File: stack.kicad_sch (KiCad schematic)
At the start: 108 parts, among them CN1 10nF, CN2 10nF, CN3 10nF, CN4 10nF, CN5 10nF, CN6 10nF, CN7 10nF, J5 CELLS, J6 TEMP0, J7 TEMP1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

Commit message: pre production
- footprints change
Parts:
- C11: footprint Capacitor_SMD:C_1206_3216Metric -> Capacitor_SMD:C_1210_3225Metric
- Fa0, Fa1, Fa10, Fa11, Fa12, Fa13, Fa14, Fa2, Fa3, Fa4, Fa5, Fa6, Fa7, Fa8, Fa9: footprint Fuse:Fuse_0805_2012Metric -> Fuse:Fuse_1206_3216Metric
- R3: footprint Resistor_SMD:R_0603_1608Metric -> Resistor_SMD:R_0805_2012Metric
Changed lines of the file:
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@@
       (effects (font (size 1.27 1.27)) hide)
     )
-    (property "Footprint" "Fuse:Fuse_0805_2012Metric" (id 2) (at 60.96 29.972 90)
+    (property "Footprint" "Fuse:Fuse_1206_3216Metric" (id 2) (at 60.96 29.972 90)
       (effects (font (size 1.27 1.27)) hide)
     )
@@
       (effects (font (size 1.27 1.27)) hide)
     )
-    (property "Footprint" "Fuse:Fuse_0805_2012Metric" (id 2) (at 38.1 32.512 90)
+    (property "Footprint" "Fuse:Fuse_1206_3216Metric" (id 2) (at 38.1 32.512 90)
       (effects (font (size 1.27 1.27)) hide)
     )
@@
       (effects (font (size 1.27 1.27)) hide)
     )
-    (property "Footprint" "Fuse:Fuse_0805_2012Metric" (id 2) (at 38.1 29.972 90)
+    (property "Footprint" "Fuse:Fuse_1206_3216Metric" (id 2) (at 38.1 29.972 90)
       (effects (font (size 1.27 1.27)) hide)
     )
@@
     (property "Reference" "R3" (id 0) (at 69.85 128.27 90))
     (property "Value" "100R" (id 1) (at 69.85 129.54 90))
-    (property "Footprint" "Resistor_SMD:R_0603_1608Metric" (id 2) (at 69.85 125.73 0)
+    (property "Footprint" "Resistor_SMD:R_0805_2012Metric" (id 2) (at 69.85 125.73 0)
       (effects (font (size 1.27 1.27)) hide)
     )
@@
       (effects (font (size 1.27 1.27)) hide)
     )
-    (property "Footprint" "Fuse:Fuse_0805_2012Metric" (id 2) (at 38.1 17.272 90)
+    (property "Footprint" "Fuse:Fuse_1206_3216Metric" (id 2) (at 38.1 17.272 90)
       (effects (font (size 1.27 1.27)) hide)
     )
@@
       (effects (font (size 1.27 1.27)) hide)
     )
-    (property "Footprint" "Fuse:Fuse_0805_2012Metric" (id 2) (at 38.1 24.892 90)
+    (property "Footprint" "Fuse:Fuse_1206_3216Metric" (id 2) (at 38.1 24.892 90)
       (effects (font (size 1.27 1.27)) hide)
     )
@@
       (effects (font (size 1.27 1.27)) hide)
     )
-    (property "Footprint" "Fuse:Fuse_0805_2012Metric" (id 2) (at 60.96 32.512 90)
+    (property "Footprint" "Fuse:Fuse_1206_3216Metric" (id 2) (at 60.96 32.512 90)
       (effects (font (size 1.27 1.27)) hide)
     )
@@
       (effects (font (size 1.27 1.27)) hide)
     )
-    (property "Footprint" "Fuse:Fuse_0805_2012Metric" (id 2) (at 60.96 19.812 90)
+    (property "Footprint" "Fuse:Fuse_1206_3216Metric" (id 2) (at 60.96 19.812 90)
       (effects (font (size 1.27 1.27)) hide)
     )
@@
       (effects (font (size 1.27 1.27)) hide)
     )
-    (property "Footprint" "Fuse:Fuse_0805_2012Metric" (id 2) (at 60.96 24.892 90)
+    (property "Footprint" "Fuse:Fuse_1206_3216Metric" (id 2) (at 60.96 24.892 90)
       (effects (font (size 1.27 1.27)) hide)
     )
@@
       (effects (font (size 1.27 1.27)) hide)
     )
-    (property "Footprint" "Fuse:Fuse_0805_2012Metric" (id 2) (at 38.1 14.732 90)
+    (property "Footprint" "Fuse:Fuse_1206_3216Metric" (id 2) (at 38.1 14.732 90)
       (effects (font (size 1.27 1.27)) hide)
     )
@@
       (effects (font (size 1.27 1.27)) hide)
     )
-    (property "Footprint" "Fuse:Fuse_0805_2012Metric" (id 2) (at 38.1 35.052 90)
+    (property "Footprint" "Fuse:Fuse_1206_3216Metric" (id 2) (at 38.1 35.052 90)
       (effects (font (size 1.27 1.27)) hide)
     )
@@
       (effects (font (size 1.27 1.27)) hide)
     )
-    (property "Footprint" "Fuse:Fuse_0805_2012Metric" (id 2) (at 38.1 22.352 90)
+    (property "Footprint" "Fuse:Fuse_1206_3216Metric" (id 2) (at 38.1 22.352 90)
       (effects (font (size 1.27 1.27)) hide)
     )
@@
       (effects (font (size 1.27 1.27)) hide)
     )
-    (property "Footprint" "Fuse:Fuse_0805_2012Metric" (id 2) (at 60.96 27.432 90)
+    (property "Footprint" "Fuse:Fuse_1206_3216Metric" (id 2) (at 60.96 27.432 90)
       (effects (font (size 1.27 1.27)) hide)
     )
@@
       (effects (font (size 1.27 1.27)) hide)
     )
-    (property "Footprint" "Fuse:Fuse_0805_2012Metric" (id 2) (at 38.1 19.812 90)
+    (property "Footprint" "Fuse:Fuse_1206_3216Metric" (id 2) (at 38.1 19.812 90)
       (effects (font (size 1.27 1.27)) hide)
     )
@@
       (effects (font (size 1.27 1.27)) (justify left))
     )
-    (property "Footprint" "Capacitor_SMD:C_1206_3216Metric" (id 2) (at 103.8352 123.19 0)
+    (property "Footprint" "Capacitor_SMD:C_1210_3225Metric" (id 2) (at 103.8352 123.19 0)
       (effects (font (size 1.27 1.27)) hide)
     )
@@
       (effects (font (size 1.27 1.27)) hide)
     )
-    (property "Footprint" "Fuse:Fuse_0805_2012Metric" (id 2) (at 60.96 22.352 90)
+    (property "Footprint" "Fuse:Fuse_1206_3216Metric" (id 2) (at 60.96 22.352 90)
       (effects (font (size 1.27 1.27)) hide)
     )
@@
       (effects (font (size 1.27 1.27)) hide)
     )
-    (property "Footprint" "Fuse:Fuse_0805_2012Metric" (id 2) (at 38.1 27.432 90)
-      (effects (font (size 1.27 1.27)) hide)
-    )
+    (property "Footprint" "Fuse:Fuse_1206_3216Metric" (id 2) (at 38.1 27.432 90)
+      (effects (font (size 1.27 1.27)) hide)
+    )

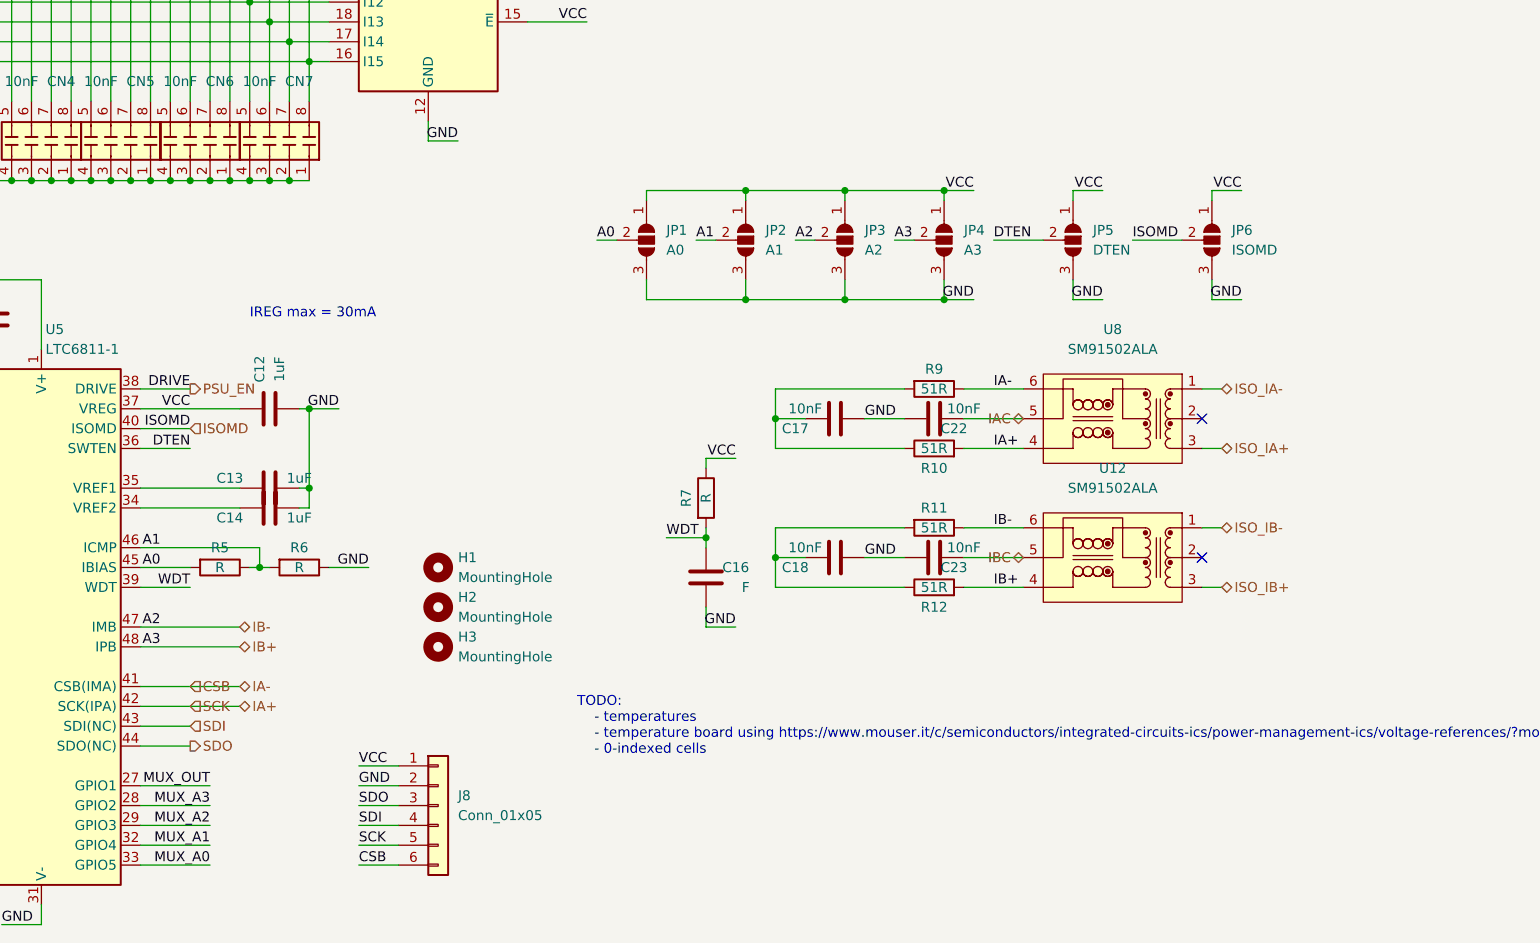
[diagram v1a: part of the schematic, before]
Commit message: production candidate
- footprint change
- added ltc6811-2 full compatibility
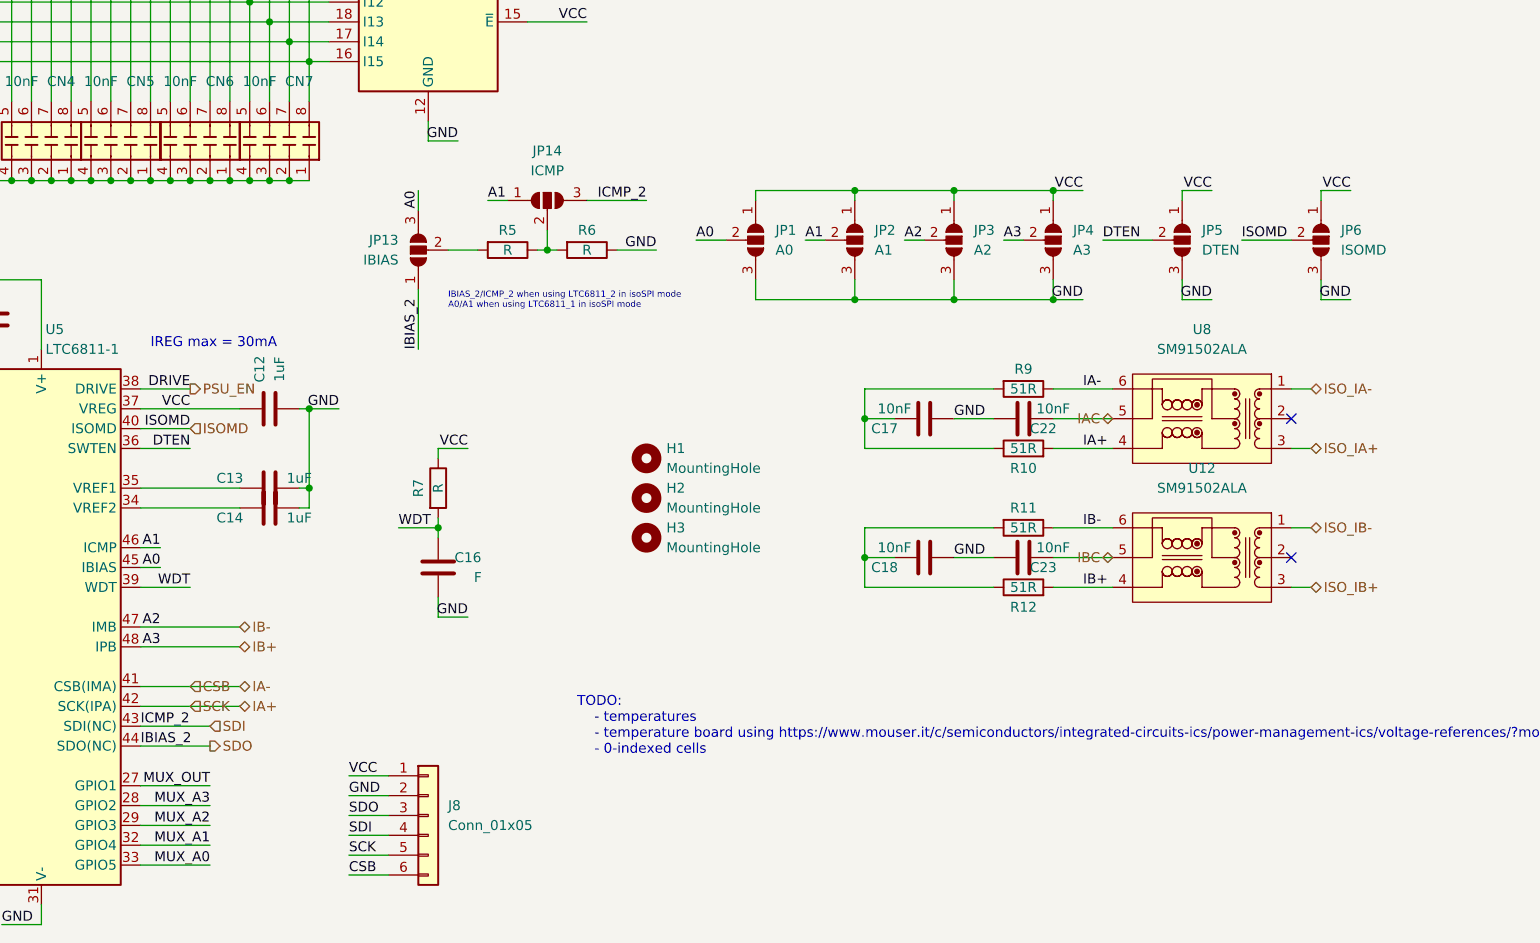
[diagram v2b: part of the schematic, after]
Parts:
- added JP13: IBIAS, Jumper:SolderJumper-3_P1.3mm_Open_RoundedPad1.0x1.5mm, symbol Jumper:SolderJumper_3_Open
- added JP14: ICMP, Jumper:SolderJumper-3_P1.3mm_Open_RoundedPad1.0x1.5mm, symbol Jumper:SolderJumper_3_Open
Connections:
- net A0: now also JP13.3 (B); no longer R5.2
- net A1: now also JP14.1 (A); no longer R5.1, R6.2
- net SDI: now also JP14.3 (B)
- net SDO: now also JP13.1 (A)
- new net: JP14.2 (C), R5.1, R6.2
- new net: JP13.2 (C), R5.2
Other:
- note added: "IBIAS_2/ICMP_2 when using LTC6811_2 in isoSPI mode A0/A1 when using LTC6811_1 in isoSPI mode"
- moved on the sheet: C16, C17, C18, C22, C23, H1, H2, H3, J8, JP1, JP2, JP3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

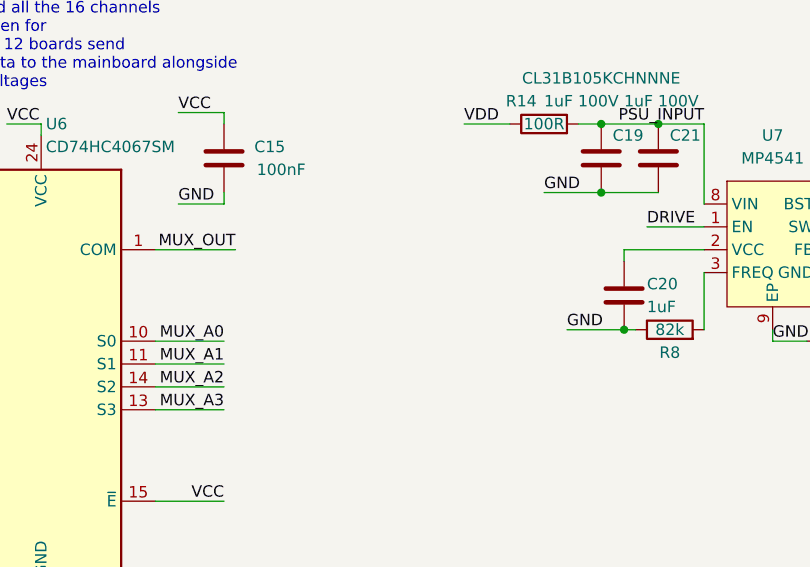
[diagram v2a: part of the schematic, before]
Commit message: fix
added ltc gpio pull up resistor
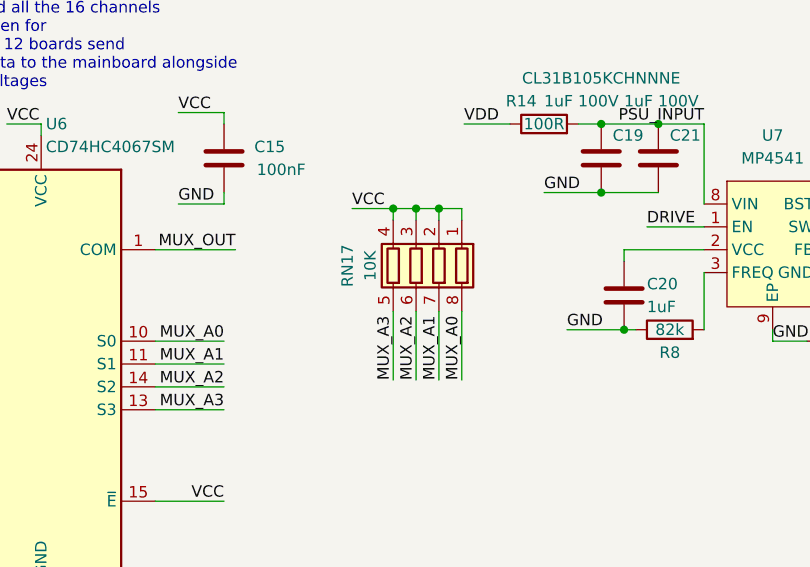
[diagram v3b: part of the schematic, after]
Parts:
- added RN17: 10K, Resistor_SMD:R_Array_Convex_4x0603, symbol Device:R_Pack04
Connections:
- net MUX_A0: now also RN17.8 (R1.2)
- net MUX_A1: now also RN17.7 (R2.2)
- net MUX_A2: now also RN17.6 (R3.2)
- net MUX_A3: now also RN17.5 (R4.2)
- net VCC: now also RN17.1 (R1.1), RN17.2 (R2.1), RN17.3 (R3.1), RN17.4 (R4.1)
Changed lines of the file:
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@@
   (junction (at 19.05 76.2) (diameter 0) (color 0 0 0 0)
   )
+  (junction (at 200.406 48.768) (diameter 0) (color 0 0 0 0)
+  )
   (junction (at 260.35 53.34) (diameter 0) (color 0 0 0 0)
   )
@@
   (junction (at 83.82 58.42) (diameter 0) (color 0 0 0 0)
   )
+  (junction (at 202.946 48.768) (diameter 0) (color 0 0 0 0)
+  )
+  (junction (at 197.866 48.768) (diameter 0) (color 0 0 0 0)
+  )
   (junction (at 143.51 140.97) (diameter 0) (color 0 0 0 0)
   )
@@
     (stroke (width 0) (type default) (color 0 0 0 0))
   )
+  (wire (pts (xy 200.406 48.768) (xy 202.946 48.768))
+    (stroke (width 0) (type default) (color 0 0 0 0))
+  )
   (wire (pts (xy 232.41 39.37) (xy 227.33 39.37))
     (stroke (width 0) (type default) (color 0 0 0 0))
@@
     (stroke (width 0) (type default) (color 0 0 0 0))
   )
+  (wire (pts (xy 205.486 48.768) (xy 205.486 50.038))
+    (stroke (width 0) (type default) (color 0 0 0 0))
+  )
   (wire (pts (xy 45.72 170.18) (xy 49.53 170.18))
     (stroke (width 0) (type default) (color 0 0 0 0))
@@
     (stroke (width 0) (type default) (color 0 0 0 0))
   )
+  (wire (pts (xy 205.486 60.198) (xy 205.486 67.818))
+    (stroke (width 0) (type default) (color 0 0 0 0))
+  )
   (wire (pts (xy 35.56 184.15) (xy 35.56 170.18))
     (stroke (width 0) (type default) (color 0 0 0 0))
@@
     (stroke (width 0) (type default) (color 0 0 0 0))
   )
+  (wire (pts (xy 193.294 48.768) (xy 197.866 48.768))
+    (stroke (width 0) (type default) (color 0 0 0 0))
+  )
   (wire (pts (xy 121.92 153.67) (xy 128.27 153.67))
     (stroke (width 0) (type default) (color 0 0 0 0))
@@
     (stroke (width 0) (type default) (color 0 0 0 0))
   )
+  (wire (pts (xy 202.946 48.768) (xy 205.486 48.768))
+    (stroke (width 0) (type default) (color 0 0 0 0))
+  )
   (wire (pts (xy 205.74 39.37) (xy 210.82 39.37))
     (stroke (width 0) (type default) (color 0 0 0 0))
@@
     (stroke (width 0) (type default) (color 0 0 0 0))
   )
+  (wire (pts (xy 200.406 60.198) (xy 200.406 67.818))
+    (stroke (width 0) (type default) (color 0 0 0 0))
+  )
   (wire (pts (xy 107.95 50.8) (xy 107.95 91.44))
     (stroke (width 0) (type default) (color 0 0 0 0))
@@
     (stroke (width 0) (type default) (color 0 0 0 0))
   )
+  (wire (pts (xy 200.406 48.768) (xy 200.406 50.038))
+    (stroke (width 0) (type default) (color 0 0 0 0))
+  )
   (wire (pts (xy 121.92 186.69) (xy 130.81 186.69))
     (stroke (width 0) (type default) (color 0 0 0 0))
@@
     (stroke (width 0) (type default) (color 0 0 0 0))
   )
+  (wire (pts (xy 197.866 48.768) (xy 200.406 48.768))
+    (stroke (width 0) (type default) (color 0 0 0 0))
+  )
   (wire (pts (xy 113.03 44.45) (xy 113.03 55.88))
     (stroke (width 0) (type default) (color 0 0 0 0))
@@
     (stroke (width 0) (type default) (color 0 0 0 0))
   )
+  (wire (pts (xy 197.866 60.198) (xy 197.866 67.818))
+    (stroke (width 0) (type default) (color 0 0 0 0))
+  )
   (wire (pts (xy 80.01 137.16) (xy 74.93 137.16))
     (stroke (width 0) (type default) (color 0 0 0 0))
@@
     (stroke (width 0) (type default) (color 0 0 0 0))
   )
+  (wire (pts (xy 202.946 48.768) (xy 202.946 50.038))
+    (stroke (width 0) (type default) (color 0 0 0 0))
+  )
   (wire (pts (xy 96.52 83.82) (xy 140.97 83.82))
     (stroke (width 0) (type default) (color 0 0 0 0))
@@
     (stroke (width 0) (type default) (color 0 0 0 0))
   )
+  (wire (pts (xy 202.946 60.198) (xy 202.946 67.818))
+    (stroke (width 0) (type default) (color 0 0 0 0))
+  )
   (wire (pts (xy 96.52 86.36) (xy 143.51 86.36))
     (stroke (width 0) (type default) (color 0 0 0 0))
@@
     (stroke (width 0) (type default) (color 0 0 0 0))
   )
+  (wire (pts (xy 197.866 48.768) (xy 197.866 50.038))
+    (stroke (width 0) (type default) (color 0 0 0 0))
+  )
   (wire (pts (xy 34.29 121.92) (xy 35.56 121.92))
     (stroke (width 0) (type default) (color 0 0 0 0))
@@
     (effects (font (size 1.27 1.27)) (justify right bottom))
   )
+  (label "MUX_A3" (at 197.866 67.818 90)
+    (effects (font (size 1.27 1.27)) (justify left bottom))
+  )
   (label "CC01" (at 77.47 34.29 180)
     (effects (font (size 1.27 1.27)) (justify right bottom))
@@
     (effects (font (size 1.27 1.27)) (justify left bottom))
   )
+  (label "MUX_A0" (at 205.486 67.818 90)
+    (effects (font (size 1.27 1.27)) (justify left bottom))
+  )
   (label "A2" (at 124.46 158.75 180)
     (effects (font (size 1.27 1.27)) (justify right bottom))
@@
     (effects (font (size 1.27 1.27)) (justify left bottom))
   )
+  (label "MUX_A1" (at 202.946 67.818 90)
+    (effects (font (size 1.27 1.27)) (justify left bottom))
+  )
   (label "C03" (at 91.44 173.99 0)
     (effects (font (size 1.27 1.27)) (justify left bottom))
@@
     (effects (font (size 1.27 1.27)) (justify right bottom))
   )
+  (label "VCC" (at 193.294 48.768 0)
+    (effects (font (size 1.27 1.27)) (justify left bottom))
+  )
   (label "C11" (at 59.69 139.7 0)
     (effects (font (size 1.27 1.27)) (justify left bottom))
@@
     (effects (font (size 1.27 1.27)) (justify right bottom))
   )
+  (label "MUX_A2" (at 200.406 67.818 90)
+    (effects (font (size 1.27 1.27)) (justify left bottom))
+  )
   (label "C04" (at 91.44 168.91 0)
     (effects (font (size 1.27 1.27)) (justify left bottom))
@@
     (pin "2")
   )
+  (symbol (lib_id "Device:R_Pack04") (at 200.406 55.118 180) (unit 1)
+    (in_bom yes) (on_board yes)
+    (property "Reference" "RN17" (id 0) (at 192.786 55.118 90))
+    (property "Value" "10K" (id 1) (at 195.326 55.118 90))
+    (property "Footprint" "Resistor_SMD:R_Array_Convex_4x0603" (id 2) (at 193.421 55.118 90)
+      (effects (font (size 1.27 1.27)) hide)
+    )
+    (property "Datasheet" "~" (id 3) (at 200.406 55.118 0)
+      (effects (font (size 1.27 1.27)) hide)
+    )
+    (pin "1")
+    (pin "2")
+    (pin "3")
+    (pin "4")
+    (pin "5")
+    (pin "6")
+    (pin "7")
+    (pin "8")
+  )
   (symbol (lib_id "Device:FerriteBead_Small") (at 24.13 36.83 270) (unit 1)
